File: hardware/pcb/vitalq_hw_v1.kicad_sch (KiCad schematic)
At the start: 27 parts, among them J1 USB-C, J2 LiPo pads, Q2 CSD13380F3, U17 MAX17048G+T10, U2 MCP73831T-2ACI/OT, U3 TPS63802DLAR, U4 TPS7A2018PDBVR

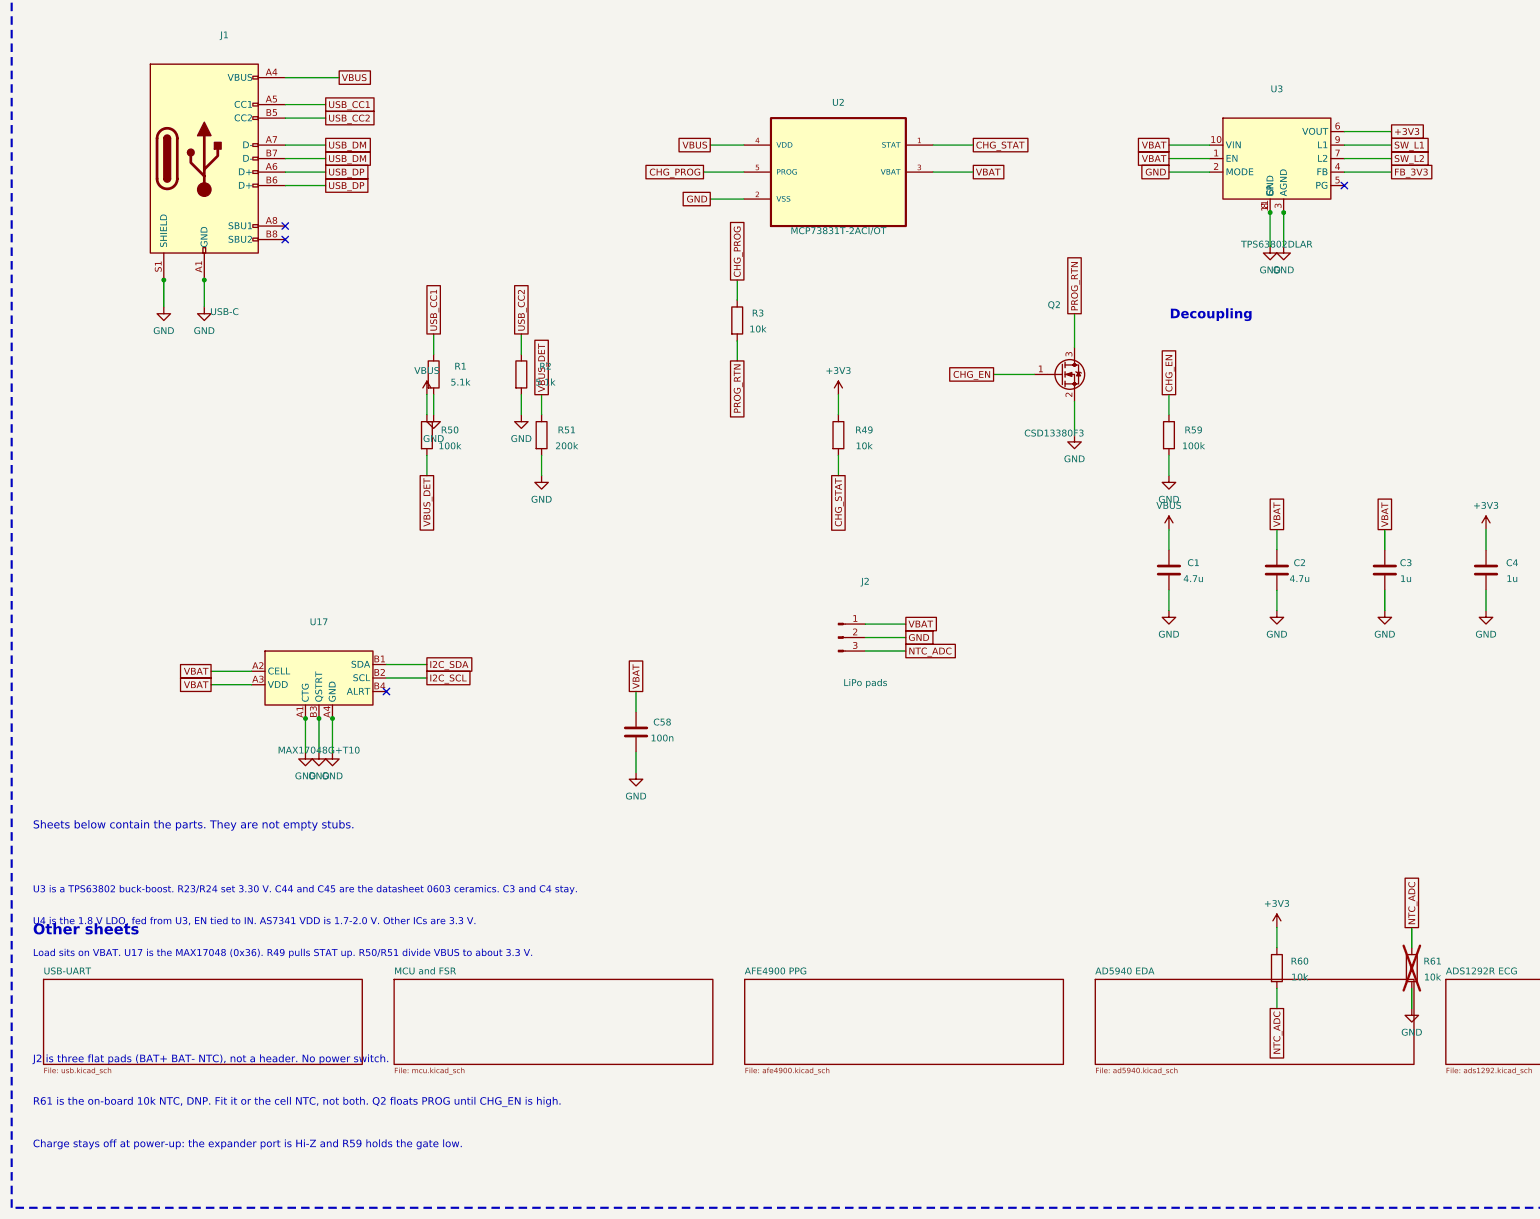
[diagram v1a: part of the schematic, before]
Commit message: Fix the review's datasheet errors without changing respiration or the GDTs.
Replace the MCP73831 with a BQ25170 so a flat cell still charges from USB, add the missing series protection and ESP32/CP2102 passives, and withdraw the claim that respiration still works with 51 kΩ in the loop.

Co-authored-by: Riyu-D1 <Riyu-D1@users.noreply.github.com>
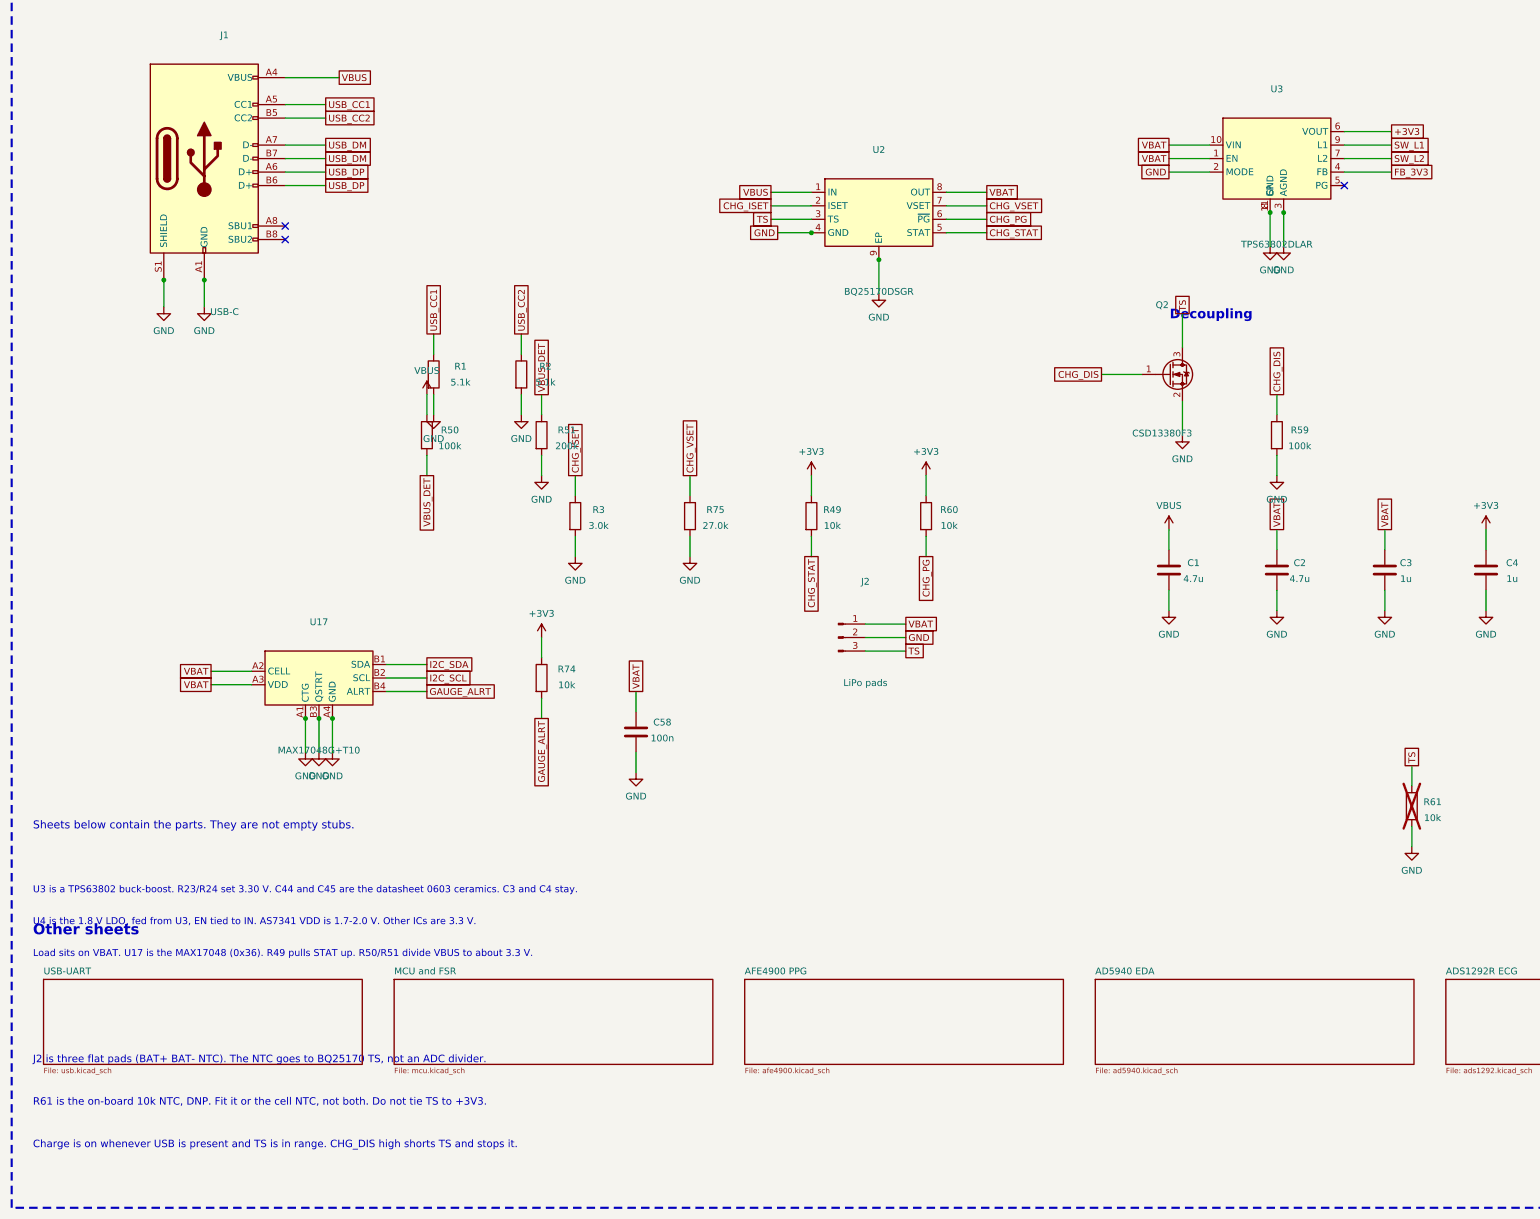
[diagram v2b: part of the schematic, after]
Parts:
- removed U2: MCP73831T-2ACI/OT, snap:SOT95P280X145-5N, symbol vitalq:MCP73831T-2ACI_OT
- added R74: 10k, Resistor_SMD:R_0402_1005Metric, symbol vitalq:R
- added R75: 27.0k, Resistor_SMD:R_0402_1005Metric, symbol vitalq:R
- added U2: BQ25170DSGR, Package_SON:Texas_DSG0008A_WSON-8-1EP_2x2mm_P0.5mm_EP0.9x1.6mm, symbol vitalq:BQ25170
- R3: value 10k -> 3.0k
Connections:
- net +3V3: now also R74.1
- net CHG_STAT: now also U2.5 (STAT)
- net GND: now also R3.2, R75.2, U2.4 (GND), U2.9 (EP)
- net VBAT: now also U2.8 (OUT)
- net VBUS: now also U2.1 (IN)
- net GAUGE_ALRT: now reaches U17.B4 (ALRT)
- net GAUGE_ALRT: now also R74.2
- net CHG_EN renamed CHG_DIS
- net CHG_PROG renamed CHG_ISET
- net CHG_ISET: now also U2.2 (ISET)
- net NTC_ADC renamed TS
- net TS: now also Q2.3 (D), U2.3 (TS); no longer R60.2
- removed net PROG_RTN: Q2.3 (D), R3.2
- new net CHG_PG: R60.2, U2.6 (~{PG})
- new net CHG_VSET: R75.1, U2.7 (VSET)
- no-connect marks 4 -> 3
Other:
- note added: "Charge is on whenever USB is present and TS is in range. CHG_DIS high shorts TS and stops it."
- note added: "J2 is three flat pads (BAT+ BAT- NTC). The NTC goes to BQ25170 TS, not an ADC divider."
- note added: "R61 is the on-board 10k NTC, DNP. Fit it or the cell NTC, not both. Do not tie TS to +3V3."
- note removed: "Charge stays off at power-up: the expander port is Hi-Z and R59 holds the gate low."
- note removed: "J2 is three flat pads (BAT+ BAT- NTC), not a header. No power switch."
- note removed: "R61 is the on-board 10k NTC, DNP. Fit it or the cell NTC, not both. Q2 floats PROG until CHG_EN is high."

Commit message: Prepare hw_v1 for prefab review without claiming the route is finished.
Add the gauge TDFN, USB ESD, sense links, test access, and JLC BOM fields, and keep the partial Freerouting result with the remaining open nets listed.

Co-authored-by: Riyu-D1 <Riyu-D1@users.noreply.github.com>
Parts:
- C1: footprint Capacitor_SMD:C_0402_1005Metric -> Capacitor_SMD:C_0603_1608Metric
- Q2: value CSD13380F3 -> CSD13380F3T
- R3: value 3.0k -> 1.5k
- U17: footprint vitalq:MAX17048_WLP -> Package_DFN_QFN:TDFN-8-1EP_2x2mm_P0.5mm_EP0.8x1.2mm
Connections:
- net GAUGE_ALRT: now also U17.5 (ALRT); no longer U17.B4 (ALRT)
- net GND: now also U17.1 (CTG), U17.4 (GND), U17.6 (QSTRT), U17.9 (EP); no longer U17.A1 (CTG), U17.A4 (GND), U17.B3 (QSTRT)
- net I2C_SCL: now also U17.7 (SCL); no longer U17.B2 (SCL)
- net I2C_SDA: now also U17.8 (SDA); no longer U17.B1 (SDA)
- net VBAT: now also U17.2 (CELL), U17.3 (VDD); no longer C44.1, U17.A2 (CELL), U17.A3 (VDD), U3.1 (EN), U3.10 (VIN)
- net +1V8 renamed +1V8_LDO
- new net VBAT_SYS: C44.1, U3.1 (EN), U3.10 (VIN)
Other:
- added sheet Test and debug (debug.kicad_sch)
- note added: "J2 is BAT+ (larger pad) BAT- NTC. The cell must have a 10k NTC and a protection PCM."
- note added: "R61 stays DNP. Fit the cell NTC, not R61 as well. R3 is 1.5k, so charge current is 200 mA."
- note removed: "J2 is three flat pads (BAT+ BAT- NTC). The NTC goes to BQ25170 TS, not an ADC divider."
- note removed: "R61 is the on-board 10k NTC, DNP. Fit it or the cell NTC, not both. Do not tie TS to +3V3."
